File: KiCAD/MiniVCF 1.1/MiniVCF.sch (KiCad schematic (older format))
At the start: 63 parts, among them J10 CV2, J11 CTRL_PANEL_CONN2, J12 MAIN_BOARD_CONN2, J3 AudioIn, J4 CV1, J5 AudioOut, J8 MAIN_BOARD_CONN, J9 CTRL_PANEL_CONN, U1 TL074, U2 TL074

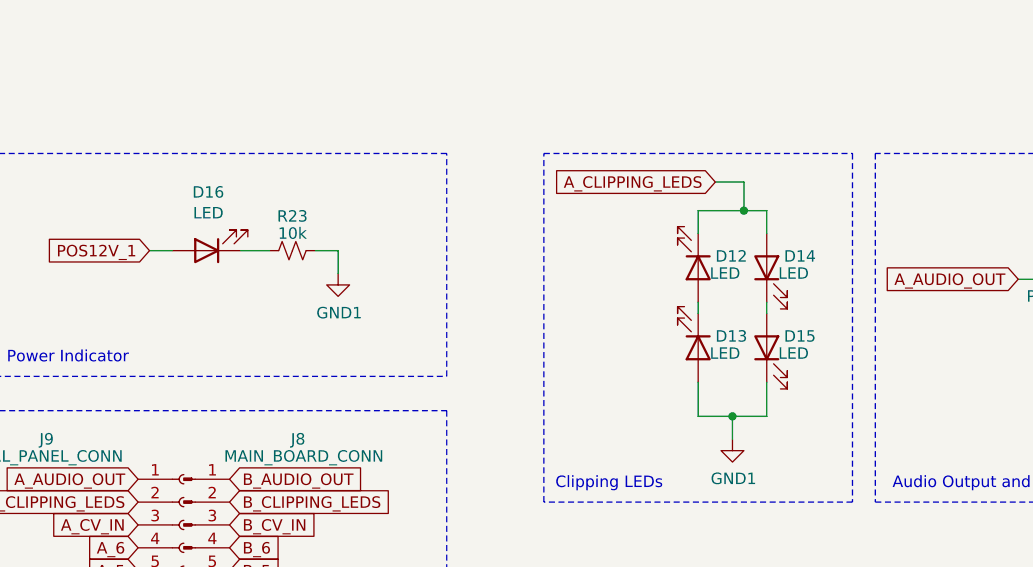
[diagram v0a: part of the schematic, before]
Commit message: added schematics export
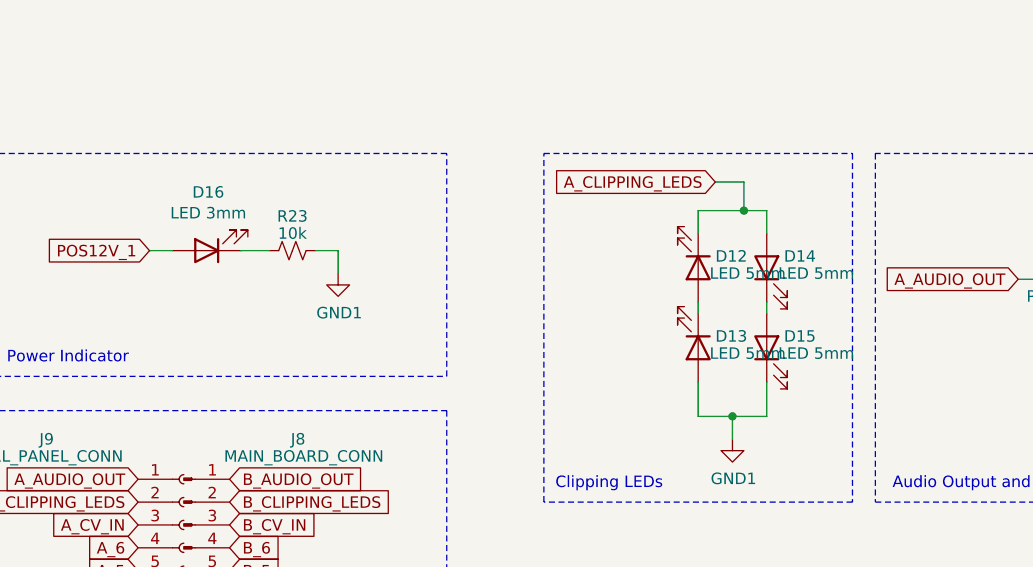
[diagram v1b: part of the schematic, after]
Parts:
- D12, D13, D14, D15: value LED -> LED 5mm
- D16: value LED -> LED 3mm
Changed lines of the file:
@@
 P 8000 5450
 F 0 "D12" V 7950 5525 50  0000 L CNN
-F 1 "LED" V 8025 5500 50  0000 L CNN
+F 1 "LED 5mm" V 8025 5500 50  0000 L CNN
 F 2 "LED_THT:LED_D5.0mm" H 8000 5450 50  0001 C CNN
 F 3 "~" H 8000 5450 50  0001 C CNN
@@
 P 8000 5800
 F 0 "D13" V 7950 5875 50  0000 L CNN
-F 1 "LED" V 8025 5850 50  0000 L CNN
+F 1 "LED 5mm" V 8025 5850 50  0000 L CNN
 F 2 "LED_THT:LED_D5.0mm" H 8000 5800 50  0001 C CNN
 F 3 "~" H 8000 5800 50  0001 C CNN
@@
 P 8300 5450
 F 0 "D14" V 8350 5375 50  0000 R CNN
-F 1 "LED" V 8275 5400 50  0000 R CNN
+F 1 "LED 5mm" V 8275 5400 50  0000 R CNN
 F 2 "LED_THT:LED_D5.0mm" H 8300 5450 50  0001 C CNN
 F 3 "~" H 8300 5450 50  0001 C CNN
@@
 P 8300 5800
 F 0 "D15" V 8350 5725 50  0000 R CNN
-F 1 "LED" V 8275 5750 50  0000 R CNN
+F 1 "LED 5mm" V 8275 5750 50  0000 R CNN
 F 2 "LED_THT:LED_D5.0mm" H 8300 5800 50  0001 C CNN
 F 3 "~" H 8300 5800 50  0001 C CNN
@@
 P 5850 5375
 F 0 "D16" H 5843 5120 50  0000 C CNN
-F 1 "LED" H 5843 5211 50  0000 C CNN
+F 1 "LED 3mm" H 5843 5211 50  0000 C CNN
 F 2 "LED_THT:LED_D3.0mm" H 5850 5375 50  0001 C CNN
 F 3 "~" H 5850 5375 50  0001 C CNN
